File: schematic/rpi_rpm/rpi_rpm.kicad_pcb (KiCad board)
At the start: 2 copper layers, 40.6 x 39.4 mm, 12 parts, among them J1 Raspberry Pi Pins, J2 PWR_SW_CONN, J3 RES_SW_CONN, J4 PWR_LED_CONN, U1 4N35, U2 4N35

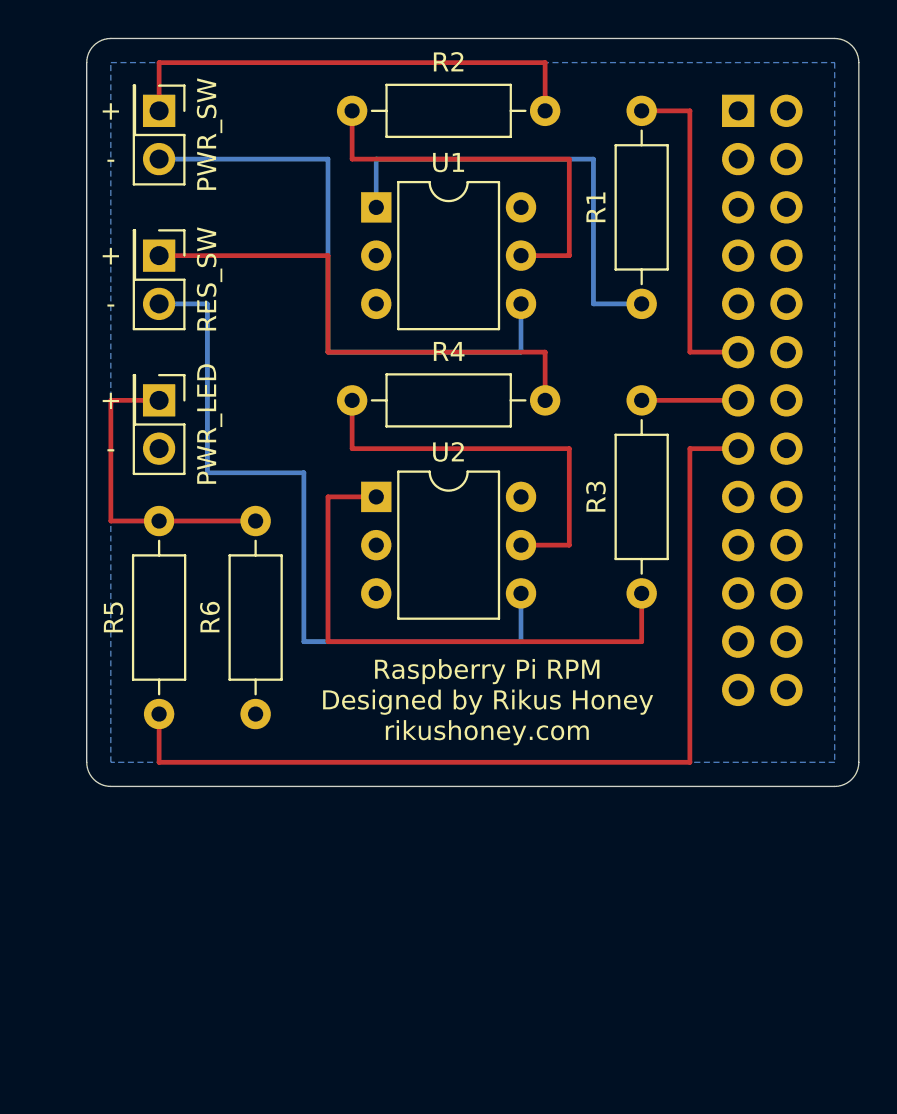
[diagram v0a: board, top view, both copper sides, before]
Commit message: Updated schematic for jumper pins
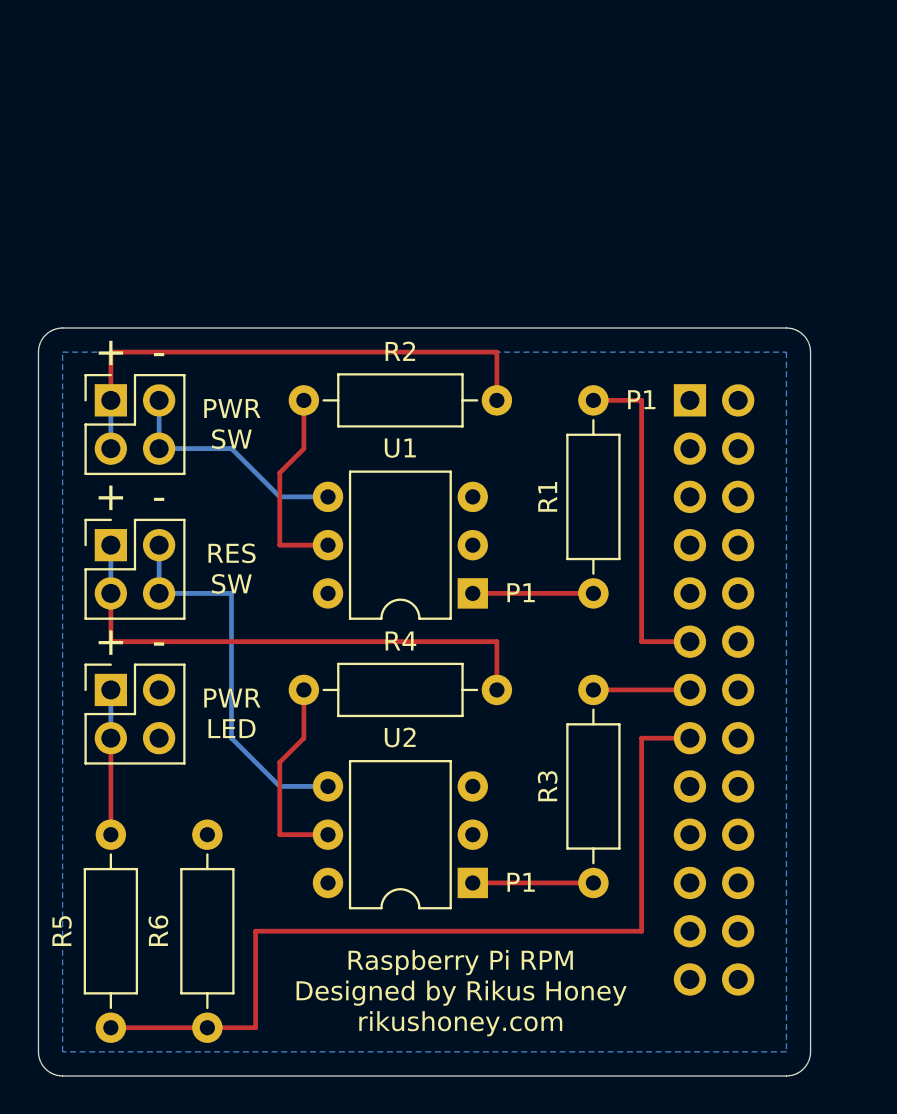
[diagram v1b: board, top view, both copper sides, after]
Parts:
- J2: value PWR_SW_CONN -> PWR_SW; footprint Connector_PinHeader_2.54mm:PinHeader_2x01_P2.54mm_Vertical -> Connector_PinHeader_2.54mm:PinHeader_2x02_P2.54mm_Vertical
- J3: value RES_SW_CONN -> RES_SW; footprint Connector_PinHeader_2.54mm:PinHeader_2x01_P2.54mm_Vertical -> Connector_PinHeader_2.54mm:PinHeader_2x02_P2.54mm_Vertical
- J4: value PWR_LED_CONN -> PWR_LED; footprint Connector_PinHeader_2.54mm:PinHeader_2x01_P2.54mm_Vertical -> Connector_PinHeader_2.54mm:PinHeader_2x02_P2.54mm_Vertical
- R1, R3: value 330R -> 220R
- moved U2 20.9 mm to (153.7, 108.0), turned to 180 degrees
- moved U1 20.9 mm to (153.7, 92.7), turned to 180 degrees
- moved J4 15.5 mm to (134.6, 97.8), turned to 0 degrees
- moved R3 15.5 mm to (160.0, 108.0)
- moved R4 15.5 mm to (154.9, 97.8)
- moved J1 15.5 mm to (165.1, 82.5)
- moved J2 15.5 mm to (134.6, 82.5), turned to 0 degrees
- moved J3 15.5 mm to (134.6, 90.2), turned to 0 degrees
- moved R1 15.5 mm to (160.0, 92.7)
- moved R2 15.5 mm to (154.9, 82.5)
- moved R6 6.84 mm to (139.7, 105.4), turned to 270 degrees
- moved R5 6.84 mm to (134.6, 105.4), turned to 270 degrees
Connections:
- R5 pad 1: PWR_LED -> Net-(J4-Pad1)
- R5 pad 2: Net-(J4-Pad1) -> PWR_LED
- R6 pad 2: Net-(J4-Pad1) -> PWR_LED
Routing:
- net Net-(R3-Pad1): track 29.2 -> 6.35 mm
- net Net-(J2-Pad2): track 31.8 -> 12.5 mm
- net Net-(J3-Pad2): track 39.4 -> 20.1 mm
- net Net-(R1-Pad1): track 24.1 -> 6.35 mm
- net Net-(R4-Pad2): track 21.6 -> 10.7 mm
- net Net-(R2-Pad2): track 21.6 -> 10.7 mm
- net Net-(J4-Pad1): track 16.5 -> 7.62 mm
- net PWR_LED: track 49.5 -> 45.7 mm
- net Net-(J2-Pad1): track 25.4 -> 27.9 mm
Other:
- board text added: "P1"
- board text added: "PWR LED"
- board text added: "PWR SW"
- board text added: "RES SW"
- board text removed: "PWR_LED"
- board text removed: "PWR_SW"
- board text removed: "RES_SW"
